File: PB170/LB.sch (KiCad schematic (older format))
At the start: 5 parts

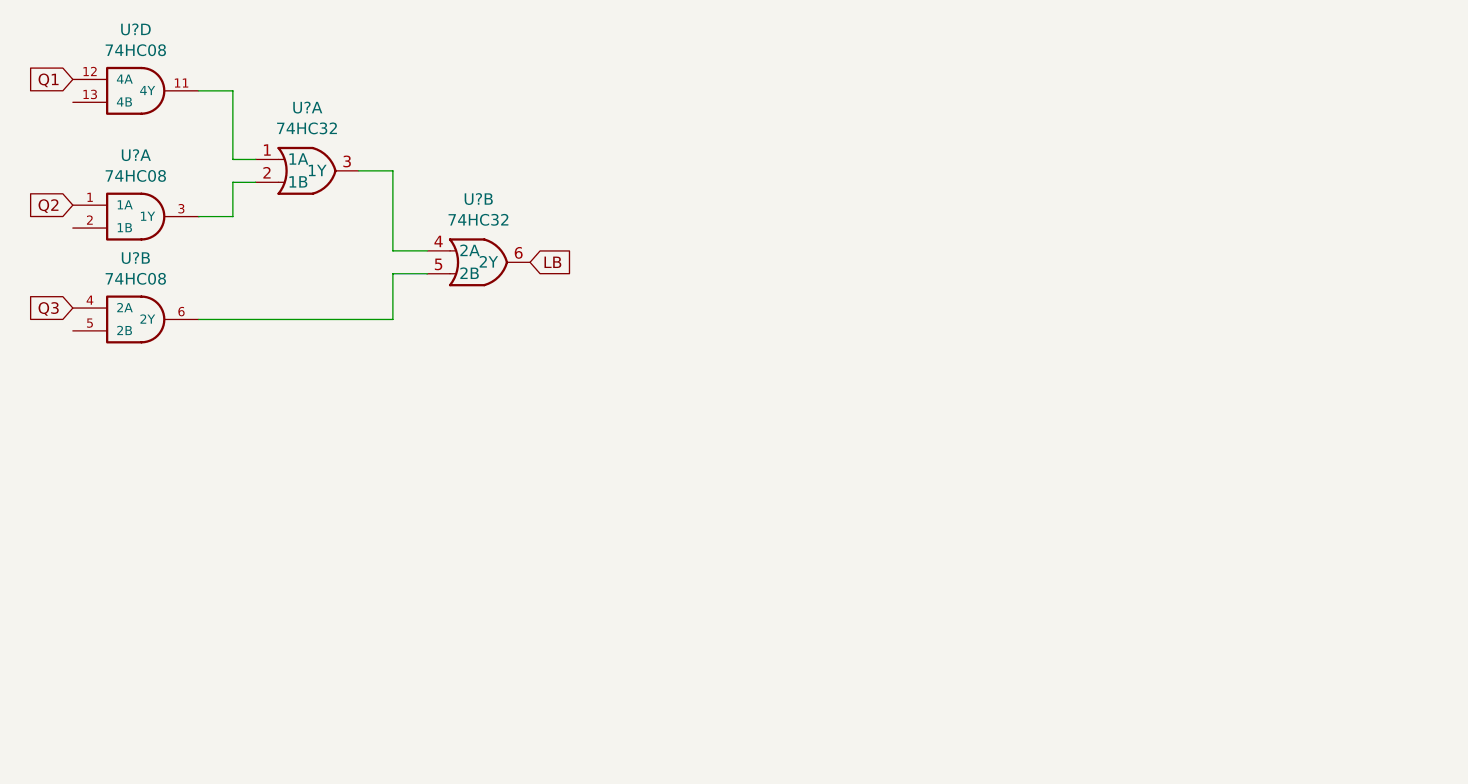
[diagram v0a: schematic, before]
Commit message: added some labels
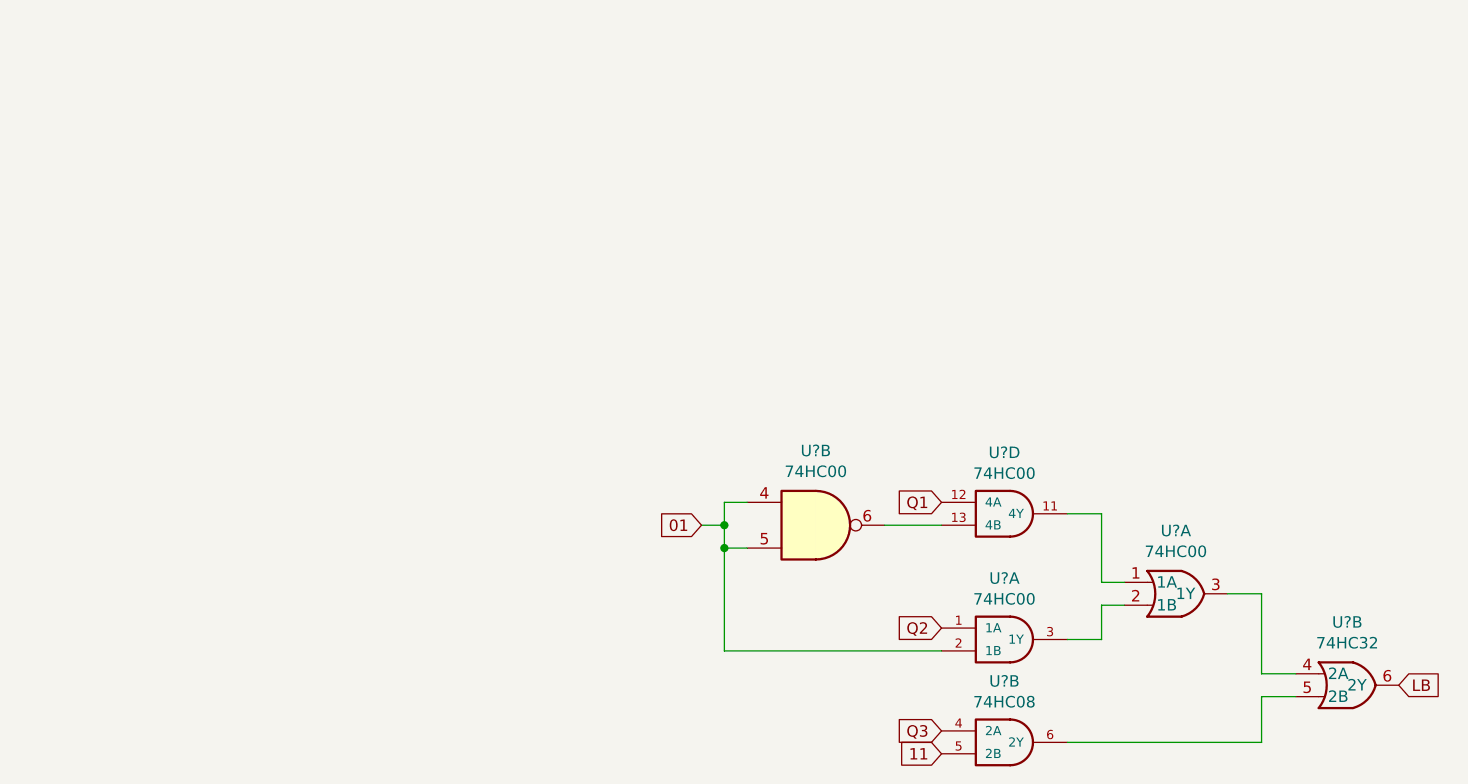
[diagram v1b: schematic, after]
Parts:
- added U?: 74HC00, Package_SO:TSSOP-14_4.4x5mm_P0.65mm, symbol 74xx:74HC00
- U?: value 74HC32 -> 74HC00; footprint Housings_SOIC:SOIC-14_3.9x8.7mm_Pitch1.27mm -> Package_SO:TSSOP-14_4.4x5mm_P0.65mm
- U? (x2): value 74HC08 -> 74HC00; footprint Housings_SOIC:SOIC-14_3.9x8.7mm_Pitch1.27mm -> Package_SO:TSSOP-14_4.4x5mm_P0.65mm
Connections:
- net at U?.13 (4B): now also U?.6
- net 01: now reaches U?.2 (1B)
- net 01: now also U?.4, U?.5
- net 11: now reaches U?.5 (2B)
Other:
- moved on the sheet: U?A, U?B, U?D
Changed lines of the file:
@@
 $Descr A4 11693 8268
 encoding utf-8
-Sheet 7 7
+Sheet 7 6
 Title ""
 Date ""
@@
 L PB170:74HC32 U?
 U 1 1 60274CEA
-P 2350 1300
-F 0 "U?" H 2325 1575 50  0000 C CNN
-F 1 "74HC32" H 2325 1484 50  0000 C CNN
-F 2 "Housings_SOIC:SOIC-14_3.9x8.7mm_Pitch1.27mm" H 1800 1500 50  0001 C CNN
-F 3 "https://datasheet.lcsc.com/szlcsc/Nexperia-74HC32D-653_C5632.pdf" H 1800 1500 50  0001 C CNN
-F 4 "C5632" H 2350 1300 50  0001 C CNN "LCSC"
-	1    2350 1300
+P 6150 3150
+F 0 "U?" H 6125 3425 50  0000 C CNN
+F 1 "74HC00" H 6125 3334 50  0000 C CNN
+F 2 "Package_SO:TSSOP-14_4.4x5mm_P0.65mm" H 5600 3350 50  0001 C CNN
+F 3 "https://datasheet.lcsc.com/szlcsc/Texas-Instruments-TI-SN74HC00PWR_C6807.pdf" H 5600 3350 50  0001 C CNN
+F 4 "C5632" H 6150 3150 50  0001 C CNN "LCSC"
+	1    6150 3150
 	1    0    0    -1
 $EndComp
@@
 L PB170:74HC32 U?
 U 2 1 60275657
-P 3100 1700
-F 0 "U?" H 3075 1975 50  0000 C CNN
-F 1 "74HC32" H 3075 1884 50  0000 C CNN
-F 2 "Housings_SOIC:SOIC-14_3.9x8.7mm_Pitch1.27mm" H 2550 1900 50  0001 C CNN
-F 3 "https://datasheet.lcsc.com/szlcsc/Nexperia-74HC32D-653_C5632.pdf" H 2550 1900 50  0001 C CNN
-F 4 "C5632" H 3100 1700 50  0001 C CNN "LCSC"
-	2    3100 1700
+P 6900 3550
+F 0 "U?" H 6875 3825 50  0000 C CNN
+F 1 "74HC32" H 6875 3734 50  0000 C CNN
+F 2 "Housings_SOIC:SOIC-14_3.9x8.7mm_Pitch1.27mm" H 6350 3750 50  0001 C CNN
+F 3 "https://datasheet.lcsc.com/szlcsc/Nexperia-74HC32D-653_C5632.pdf" H 6350 3750 50  0001 C CNN
+F 4 "C5632" H 6900 3550 50  0001 C CNN "LCSC"
+	2    6900 3550
 	1    0    0    -1
 $EndComp
@@
 L PB170:74HC08 U?
 U 4 1 60276968
-P 1550 950
-F 0 "U?" H 1575 1217 50  0000 C CNN
-F 1 "74HC08" H 1575 1126 50  0000 C CNN
-F 2 "Housings_SOIC:SOIC-14_3.9x8.7mm_Pitch1.27mm" H 1550 950 50  0001 C CNN
-F 3 "https://datasheet.lcsc.com/szlcsc/Nexperia-74HC08D-653_C5593.pdf" H 1550 950 50  0001 C CNN
-F 4 "C5593" H 1550 950 50  0001 C CNN "LCSC"
-	4    1550 950
+P 5350 2800
+F 0 "U?" H 5375 3067 50  0000 C CNN
+F 1 "74HC00" H 5375 2976 50  0000 C CNN
+F 2 "Package_SO:TSSOP-14_4.4x5mm_P0.65mm" H 5350 2800 50  0001 C CNN
+F 3 "https://datasheet.lcsc.com/szlcsc/Texas-Instruments-TI-SN74HC00PWR_C6807.pdf" H 5350 2800 50  0001 C CNN
+F 4 "C5593" H 5350 2800 50  0001 C CNN "LCSC"
+	4    5350 2800
 	1    0    0    -1
 $EndComp
@@
 L PB170:74HC08 U?
 U 1 1 602794EB
-P 1550 1500
-F 0 "U?" H 1575 1767 50  0000 C CNN
-F 1 "74HC08" H 1575 1676 50  0000 C CNN
-F 2 "Housings_SOIC:SOIC-14_3.9x8.7mm_Pitch1.27mm" H 1550 1500 50  0001 C CNN
-F 3 "https://datasheet.lcsc.com/szlcsc/Nexperia-74HC08D-653_C5593.pdf" H 1550 1500 50  0001 C CNN
-F 4 "C5593" H 1550 1500 50  0001 C CNN "LCSC"
-	1    1550 1500
+P 5350 3350
+F 0 "U?" H 5375 3617 50  0000 C CNN
+F 1 "74HC00" H 5375 3526 50  0000 C CNN
+F 2 "Package_SO:TSSOP-14_4.4x5mm_P0.65mm" H 5350 3350 50  0001 C CNN
+F 3 "https://datasheet.lcsc.com/szlcsc/Texas-Instruments-TI-SN74HC00PWR_C6807.pdf" H 5350 3350 50  0001 C CNN
+F 4 "C5593" H 5350 3350 50  0001 C CNN "LCSC"
+	1    5350 3350
 	1    0    0    -1
 $EndComp
@@
 L PB170:74HC08 U?
 U 2 1 6027A394
-P 1550 1950
-F 0 "U?" H 1575 2217 50  0000 C CNN
-F 1 "74HC08" H 1575 2126 50  0000 C CNN
-F 2 "Housings_SOIC:SOIC-14_3.9x8.7mm_Pitch1.27mm" H 1550 1950 50  0001 C CNN
-F 3 "https://datasheet.lcsc.com/szlcsc/Nexperia-74HC08D-653_C5593.pdf" H 1550 1950 50  0001 C CNN
-F 4 "C5593" H 1550 1950 50  0001 C CNN "LCSC"
-	2    1550 1950
+P 5350 3800
+F 0 "U?" H 5375 4067 50  0000 C CNN
+F 1 "74HC08" H 5375 3976 50  0000 C CNN
+F 2 "Housings_SOIC:SOIC-14_3.9x8.7mm_Pitch1.27mm" H 5350 3800 50  0001 C CNN
+F 3 "https://datasheet.lcsc.com/szlcsc/Nexperia-74HC08D-653_C5593.pdf" H 5350 3800 50  0001 C CNN
+F 4 "C5593" H 5350 3800 50  0001 C CNN "LCSC"
+	2    5350 3800
 	1    0    0    -1
 $EndComp
 Wire Wire Line
-	1850 950  2000 950
+	5650 2800 5800 2800
 Wire Wire Line
-	2000 950  2000 1250
+	5800 2800 5800 3100
 Wire Wire Line
-	2000 1250 2100 1250
+	5800 3100 5900 3100
 Wire Wire Line
-	1850 1500 2000 1500
+	5650 3350 5800 3350
 Wire Wire Line
-	2000 1500 2000 1350
+	5800 3350 5800 3200
 Wire Wire Line
-	2000 1350 2100 1350
+	5800 3200 5900 3200
 Wire Wire Line
-	1850 1950 2700 1950
+	5650 3800 6500 3800
 Wire Wire Line
-	2700 1950 2700 1750
+	6500 3800 6500 3600
 Wire Wire Line
-	2700 1750 2850 1750
+	6500 3600 6650 3600
 Wire Wire Line
-	2550 1300 2700 1300
+	6350 3150 6500 3150
 Wire Wire Line
-	2700 1300 2700 1650
+	6500 3150 6500 3500
 Wire Wire Line
-	2700 1650 2850 1650
-Text GLabel 1300 900  0    50   Input ~ 0
+	6500 3500 6650 3500
+Text GLabel 5100 2750 0    50   Input ~ 0
 Q1
-Text GLabel 1300 1450 0    50   Input ~ 0
+Text GLabel 5100 3300 0    50   Input ~ 0
 Q2
-Text GLabel 1300 1900 0    50   Input ~ 0
+Text GLabel 5100 3750 0    50   Input ~ 0
 Q3
-Text GLabel 3300 1700 2    50   Input ~ 0
+Text GLabel 7100 3550 2    50   Input ~ 0
 LB
+$Comp
+L 74xx:74HC00 U?
+U 2 1 60274732
+P 4550 2850
+AR Path="/6026D736/60274732" Ref="U?"  Part="1"
+AR Path="/6026DE84/60274732" Ref="U?"  Part="2"
+F 0 "U?" H 4550 3175 50  0000 C CNN
+F 1 "74HC00" H 4550 3084 50  0000 C CNN
+F 2 "Package_SO:TSSOP-14_4.4x5mm_P0.65mm" H 4550 2850 50  0001 C CNN
+F 3 "https://datasheet.lcsc.com/szlcsc/Texas-Instruments-TI-SN74HC00PWR_C6807.pdf" H 4550 2850 50  0001 C CNN
+F 4 "C6807" H 4550 2850 50  0001 C CNN "LCSC"
+	2    4550 2850
+	1    0    0    -1
+$EndComp
+Wire Wire Line
+	5100 2850 4850 2850
+Wire Wire Line
+	4250 2750 4150 2750
+Wire Wire Line
+	4150 2750 4150 2850
+Wire Wire Line
+	4150 2950 4250 2950
+Wire Wire Line
+	4150 2850 4050 2850
+Connection ~ 4150 2850
+Wire Wire Line
+	4150 2850 4150 2950
+Text GLabel 4050 2850 0    50   Input ~ 0
+01
+Wire Wire Line
+	4150 3400 5100 3400
+Connection ~ 4150 2950
+Wire Wire Line
+	4150 2950 4150 3400
+Text GLabel 5100 3850 0    50   Input ~ 0
+11
 $EndSCHEMATC
